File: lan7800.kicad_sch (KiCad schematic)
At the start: 6 parts

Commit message: LAN7800 update 0710
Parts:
- removed C?: 10uF, symbol Device:C
- added C?: 0.1uF, symbol Device:C
- added C?: 10uF, symbol Device:C
- added C?: 1uF, symbol Device:C
- added TP? (x5): TestPoint, symbol Connector:TestPoint
- R? (x2): Precision (none) -> 1%
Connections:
- net +1V2: now also TP?.1
- net VDD_IN: no longer U?.20 (VDDVARIO)
- net VSS: now also C?.2, TP?.1
- net +2V5: now reaches U?.12 (VDD25A)
- net +2V5: now also U?.3 (VDD25A), U?.45 (VDD25_REG_OUT), U?.6 (VDD25A), U?.9 (VDD25A), C?.1, TP?.1
- net USB2_DP: now reaches U?.26 (USB2_DP)
- net USB2_DM: now reaches U?.27 (USB2_DM)
- net USB3_TXDP: now reaches U?.28 (USB3_TXDP)
- net USB3_TXDM: now reaches U?.29 (USB3_TXDM)
- net USB3_RXDP: now reaches U?.31 (USB3_RXDP)
- net USB3_RXDM: now reaches U?.32 (USB3_RXDM)
- removed net 3V3: U?.14 (VDD_SW_IN), U?.38 (VDD33A), U?.46 (VDD33_REG_IN)
- new net +3V3: TP?.1, U?.14 (VDD_SW_IN)
- new net VDDA: TP?.1, U?.20 (VDDVARIO)
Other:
- note added: "VDD33_SW_IN"
- moved on the sheet: C?, L?, R?

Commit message: finish datalink
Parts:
- added C? (x2): 16pF, symbol Device:C_Small
- added C?: 0.1uF, symbol Device:C
- added C?: 22uF, symbol Device:C
- added C?: 1uF, symbol Device:C
- added C?: 0.1uF, symbol Device:C_Small
- added FB? (x3): 120R, symbol Device:FerriteBead_Small
- added R? (x2): 10k, symbol Device:R
- added R? (x4): 10k, symbol Device:R_Small
- added TP?: TestPoint_Small, symbol Connector:TestPoint_Small
- added U?: 93AA66C, symbol Memory_EEPROM:93AAxxC
- added Y?: 25MHz, symbol Device:Crystal_GND2_Small
- C?: Voltage 25V -> (none)
- C?: Voltage (none) -> 16V
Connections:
- net VDD_IN is gone; now on net VDDA: U?.36 (VDDVARIO), U?.39 (VDDVARIO)
- net +1V2: now also C?.1, C?.1, FB?.2, FB?.2, FB?.2; no longer U?.25 (VDD12A), U?.30 (VDD12A), U?.44 (VDD12A)
- net +3V3: now also C?.1, C?.1, U?.38 (VDD33A), U?.46 (VDD33_REG_IN), C?.1, C?.2, R?.1, R?.1, R?.2, U?.8 (VCC)
- net VSS: now also C?.2, C?.2, C?.1, C?.2, C?.2, C?.2, C?.2, C?.2, R?.2, R?.2, R?.2, U?.5 (GND), Y?.2
- net EECS: now reaches U?.16 (EECS/GPIO0)
- net EECS: now also R?.1, U?.1 (CS)
- net EEDI: now reaches U?.17 (EEDI/GPIO1)
- net EEDI: now also U?.4 (DO)
- net EEDO: now reaches U?.18 (EEDO/LED0/GPIO2)
- net EEDO: now also U?.3 (DI)
- net EECLK: now reaches U?.19 (EECLK/LED1/GPIO3)
- net EECLK: now also U?.2 (SCLK)
- net at U?.22 (PME_N/GPIO4): now also R?.2
- net at U?.23 (VBUS_DET): now also R?.2
- net LED2: now reaches U?.24 (SUSPEND_N/LED2/GPIO5)
- net LED3: now reaches U?.33 (LED3/GPIO6)
- net at U?.34 (TEST): now also R?.1
- net at U?.35 (RESET_N/PME_CLEAR): now also R?.1
- net at U?.40 (XI): now also C?.1, Y?.1
- net at U?.41 (XO): now also C?.1, Y?.3
- net at U?.43 (PME_MODE/GPIO7): now also TP?.1
- new net: R?.1, U?.6 (ORG)
- new net: FB?.1, U?.44 (VDD12A)
- new net: FB?.1, U?.30 (VDD12A)
- new net: FB?.1, U?.25 (VDD12A)
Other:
- note added: "Near PIN"
- moved on the sheet: C?, L?, R?, U?

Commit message: change 20220714, update datalink
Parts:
- removed C? (x2): 0.1uF, symbol Device:C
- removed C?: 22uF, symbol Device:C
- removed C?: 10uF, symbol Device:C
- removed C?: 1uF, symbol Device:C
- removed L?: 3.3uH, symbol pspice:INDUCTOR
- removed R?: 2k, symbol Device:R
- added C?: 10uF, symbol Device:C_Small
- added C? (x2): 0.1uF, symbol Device:C_Small
- added C?: 22uF, symbol Device:C_Small
- added C?: 1uF, symbol Device:C_Small
- added L?: 3.3uH, symbol Device:L_Small
- added R?: 2k, symbol Device:R_Small
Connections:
- net +1V2: now also C?.1, C?.1, L?.1
- net +3V3: now also C?.1, C?.1
- net VSS: now also C?.2, C?.2, C?.2, C?.2, C?.2, R?.2
- net at U?.47 (REF_REXT): now also R?.1
- net at U?.48 (REF_FILT): now also C?.1
- net at U?.13 (SW_OUT): now also L?.2
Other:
- note added: "Duplex/Collision"
- note added: "LINK/ACT"

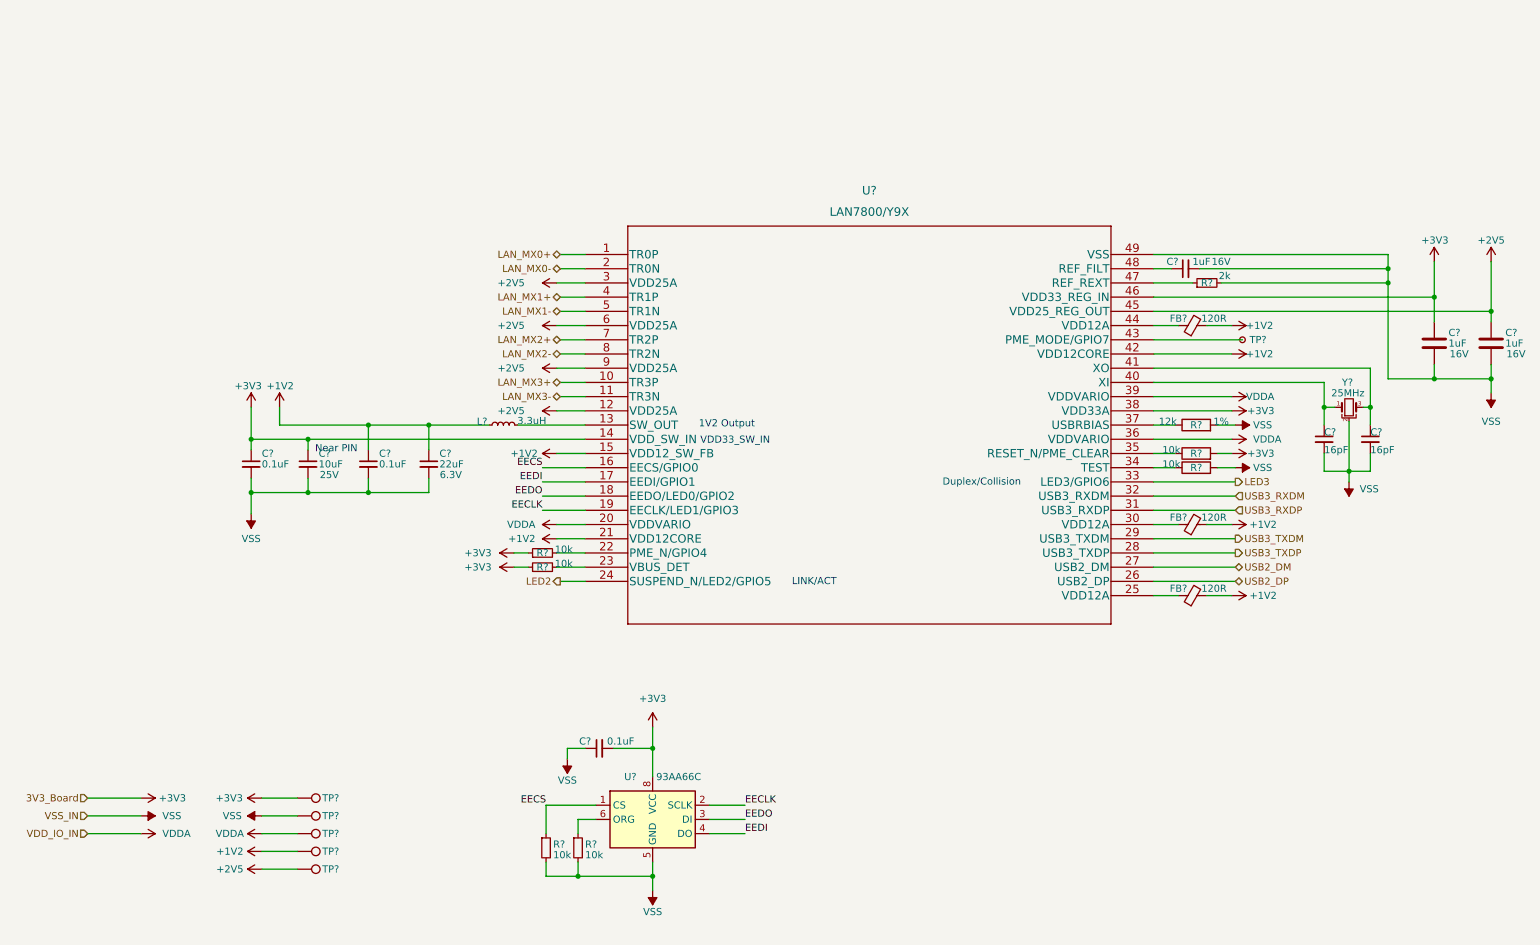
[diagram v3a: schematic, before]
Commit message: PoE TR change to 7490220122; updated pwr net
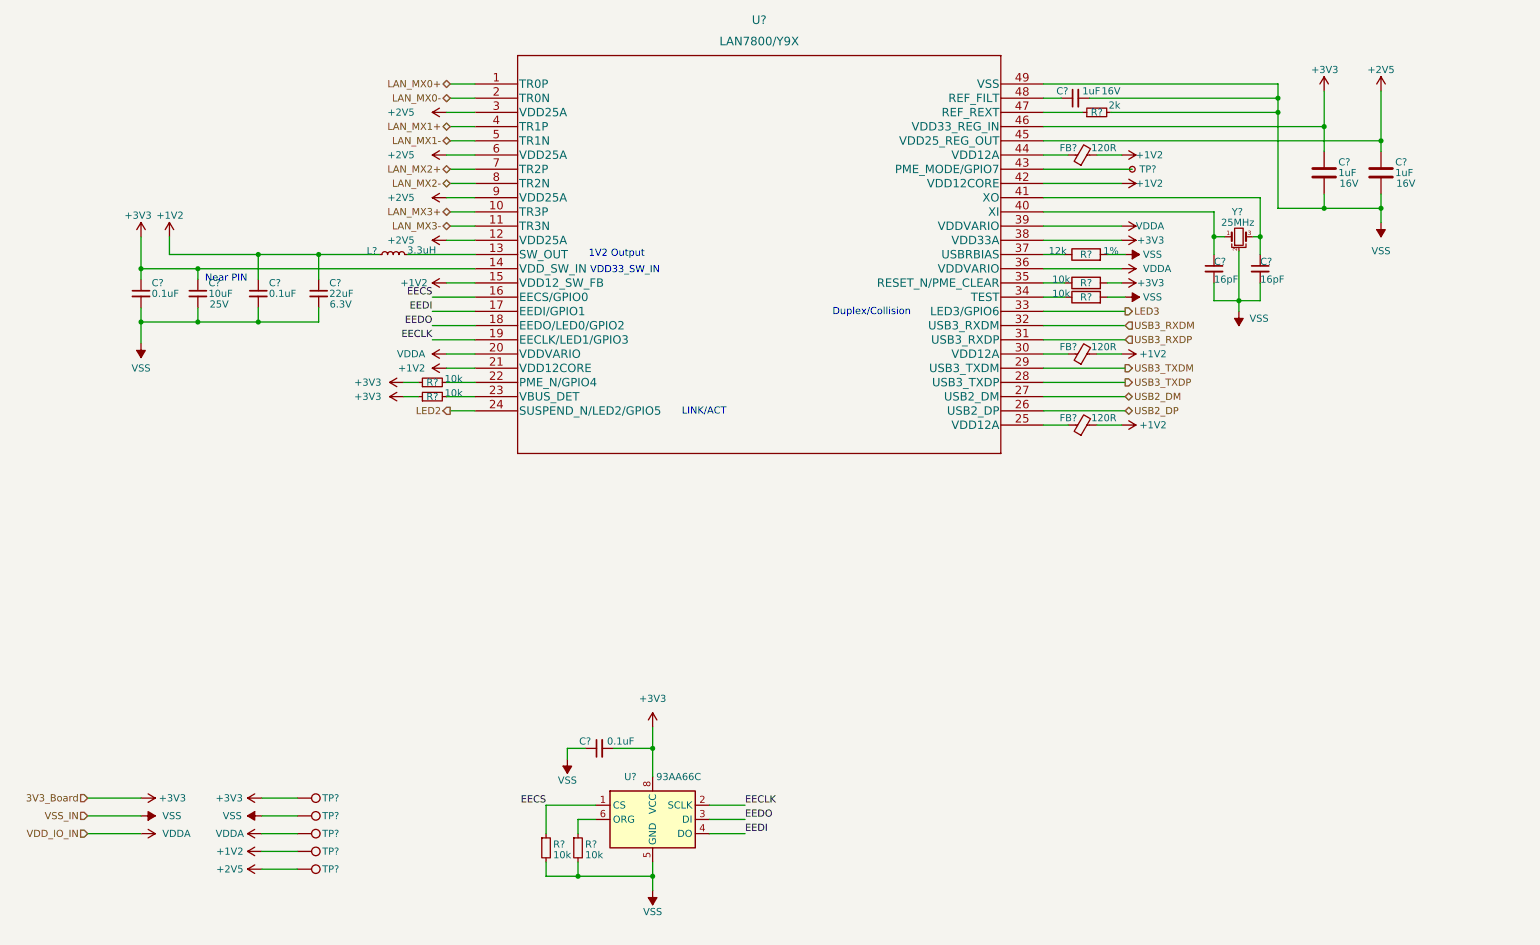
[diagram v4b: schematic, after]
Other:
- moved on the sheet: C?, FB?, L?, R?, TP?, U?, Y?

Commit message: power symbol updated
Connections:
- net +1V2 renamed 1V2
- net +2V5 renamed 2V5
- net +3V3 renamed 3V3_Board
- net VDDA renamed VDD_IO_IN
- net VSS renamed VSS_IN
